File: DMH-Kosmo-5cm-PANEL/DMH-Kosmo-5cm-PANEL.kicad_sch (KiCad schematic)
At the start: 4 parts

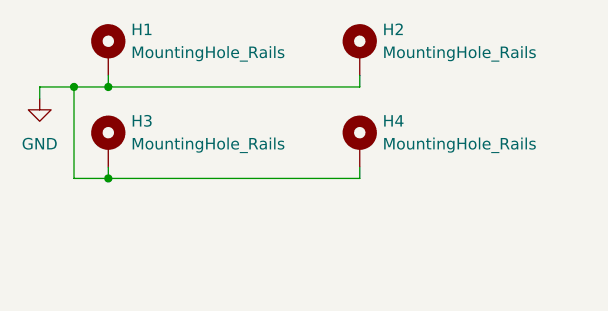
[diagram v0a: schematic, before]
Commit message: Updated 5cm and 10 templates
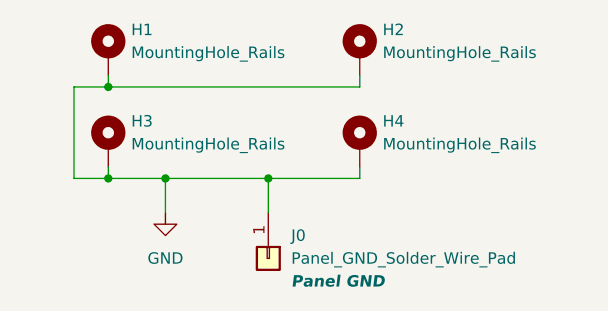
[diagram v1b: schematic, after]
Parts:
- added J0: Panel_GND_Solder_Wire_Pad, SynthStuff:Panel_GND_SolderWirePad_5x10mm, symbol SynthStuff:Panel_GND_Solder_Wire_Pad
- H1, H2, H3, H4: footprint SynthStuff:MountingHole_Slotted_Rails -> SynthStuff:MountingHole_Rails
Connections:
- net GND: now also J0.1 (Pin_1)
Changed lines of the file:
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@@
+	)
+	(junction
+		(at 34.29 269.24)
+		(diameter 0)
+		(color 0 0 0 0)
+	)
+	(junction
+		(at 45.72 269.24)
+		(diameter 0)
+		(color 0 0 0 0)
 	)
 	(junction
@@
 		(color 0 0 0 0)
 	)
-	(junction
-		(at 24.13 259.08)
-		(diameter 0)
-		(color 0 0 0 0)
-	)
-	(wire
-		(pts
-			(xy 55.88 259.08) (xy 27.94 259.08)
-		)
-		(stroke
-			(width 0)
-			(type default)
-		)
-	)
 	(wire
 		(pts
@@
 	(wire
 		(pts
-			(xy 20.32 259.08) (xy 24.13 259.08)
+			(xy 27.94 259.08) (xy 55.88 259.08)
 		)
 		(stroke
@@
 	(wire
 		(pts
-			(xy 20.32 260.35) (xy 20.32 259.08)
-		)
-		(stroke
-			(width 0)
-			(type default)
-		)
-	)
-	(wire
-		(pts
-			(xy 24.13 259.08) (xy 27.94 259.08)
+			(xy 45.72 269.24) (xy 45.72 273.05)
+		)
+		(stroke
+			(width 0)
+			(type default)
+		)
+	)
+	(wire
+		(pts
+			(xy 34.29 269.24) (xy 34.29 273.05)
 		)
 		(stroke
@@
 	(wire
 		(pts
+			(xy 45.72 269.24) (xy 34.29 269.24)
+		)
+		(stroke
+			(width 0)
+			(type default)
+		)
+	)
+	(wire
+		(pts
+			(xy 27.94 259.08) (xy 24.13 259.08)
+		)
+		(stroke
+			(width 0)
+			(type default)
+		)
+	)
+	(wire
+		(pts
 			(xy 27.94 259.08) (xy 27.94 257.81)
 		)
@@
 	(wire
 		(pts
-			(xy 55.88 269.24) (xy 27.94 269.24)
+			(xy 55.88 269.24) (xy 45.72 269.24)
+		)
+		(stroke
+			(width 0)
+			(type default)
+		)
+	)
+	(wire
+		(pts
+			(xy 34.29 269.24) (xy 27.94 269.24)
 		)
 		(stroke
@@
 			)
 		)
-		(property "Footprint" "SynthStuff:MountingHole_Slotted_Rails"
+		(property "Footprint" "SynthStuff:MountingHole_Rails"
 			(at 55.88 255.27 0)
 			(effects
@@
 	(symbol
 		(lib_id "power:GND")
-		(at 20.32 260.35 0)
+		(at 34.29 273.05 0)
 		(unit 1)
 		(exclude_from_sim no)
@@
 		(fields_autoplaced yes)
 		(property "Reference" "#PWR01"
-			(at 20.32 266.7 0)
+			(at 34.29 279.4 0)
 			(effects
 				(font
@@
 		)
 		(property "Value" "GND"
-			(at 20.32 265.43 0)
+			(at 34.29 278.13 0)
 			(effects
 				(font
@@
 		)
 		(property "Footprint" ""
-			(at 20.32 260.35 0)
+			(at 34.29 273.05 0)
 			(effects
 				(font
@@
 		)
 		(property "Datasheet" ""
-			(at 20.32 260.35 0)
+			(at 34.29 273.05 0)
 			(effects
 				(font
@@
 		)
 		(property "Description" "Power symbol creates a global label with name \"GND\" , ground"
-			(at 20.32 260.35 0)
+			(at 34.29 273.05 0)
 			(effects
 				(font
@@
 			)
 		)
-		(property "Footprint" "SynthStuff:MountingHole_Slotted_Rails"
+		(property "Footprint" "SynthStuff:MountingHole_Rails"
 			(at 27.94 265.43 0)
 			(effects
@@
 			)
 		)
-		(property "Footprint" "SynthStuff:MountingHole_Slotted_Rails"
+		(property "Footprint" "SynthStuff:MountingHole_Rails"
 			(at 55.88 265.43 0)
 			(effects
@@
 				(path "/a552705f-a9fe-462e-9913-5cfcc08b233c"
 					(reference "H4")
+					(unit 1)
+				)
+			)
+		)
+	)
+	(symbol
+		(lib_id "SynthStuff:Panel_GND_Solder_Wire_Pad")
+		(at 45.72 278.13 270)
+		(unit 1)
+		(exclude_from_sim no)
+		(in_bom no)
+		(on_board yes)
+		(dnp no)
+		(fields_autoplaced yes)
+		(property "Reference" "J0"
+			(at 48.26 275.5899 90)
+			(effects
+				(font
+					(size 1.27 1.27)
+				)
+				(justify left)
+			)
+		)
+		(property "Value" "Panel_GND_Solder_Wire_Pad"
+			(at 48.26 278.1299 90)
+			(effects
+				(font
+					(size 1.27 1.27)
+				)
+				(justify left)
+			)
+		)
+		(property "Footprint" "SynthStuff:Panel_GND_SolderWirePad_5x10mm"
+			(at 45.72 278.13 0)
+			(effects
+				(font
+					(size 1.27 1.27)
+				)
+				(hide yes)
+			)
+		)
+		(property "Datasheet" "~"
+			(at 45.72 278.13 0)
+			(effects
+				(font
+					(size 1.27 1.27)
+				)
+				(hide yes)
+			)
+		)
+		(property "Description" "Solder pad to allow connection between PCB and Front Panel"
+			(at 45.72 278.13 0)
+			(effects
+				(font
+					(size 1.27 1.27)
+				)
+				(hide yes)
+			)
+		)
+		(property "Function" "Panel GND"
+			(at 48.26 280.67 90)
+			(effects
+				(font
+					(size 1.27 1.27)
+					(thickness 0.254)
+					(bold yes)
+					(italic yes)
+				)
+				(justify left)
+			)
+		)
+		(pin "1"
+		)
+		(instances
+			(project ""
+				(path "/a552705f-a9fe-462e-9913-5cfcc08b233c"
+					(reference "J0")
 					(unit 1)
 				)
@@
 			)
 		)
-		(property "Footprint" "SynthStuff:MountingHole_Slotted_Rails"
+		(property "Footprint" "SynthStuff:MountingHole_Rails"
 			(at 27.94 255.27 0)
 			(effects
